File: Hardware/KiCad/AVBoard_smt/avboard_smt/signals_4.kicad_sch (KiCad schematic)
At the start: 20 parts, among them IC2_AUD0 7432N, IC4_AUD0 7400N, IC6_AUD0 7474N, IC7_AUD0 LM358N, U1 W65C02SP

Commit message: update kicad SMT BOMs
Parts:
- AUDJACK0: MPN RCJ-103 -> RCJ-013
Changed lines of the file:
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@@
       (effects (font (size 1.27 1.27)) hide)
     )
-    (property "MPN" "RCJ-103" (at 528.32 43.18 0)
+    (property "MPN" "RCJ-013" (at 528.32 43.18 0)
       (effects (font (size 1.27 1.27)) hide)
     )

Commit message: collect production documents for quoting
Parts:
- MOTHERBOARD0: footprint Connector_FFC-FPC:TE_4-1734839-0_1x40-1MP_P0.5mm_Horizontal -> SamacSys_Parts:F34G1A7Q1E8C40; MPN 4-1734839-0 -> F34G-1A7Q1-E8C40

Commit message: replace dual ported frame buffer with mirrored single ported rams
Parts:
- removed unit 4 of IC2_AUD0
- added IC2: IS61C64AL-10TLI, SOP55P1340X120-28N, symbol SamacSys_Parts:IS61C64AL-10TLI
- added IC3: SN74CBT16245CDGGR, SOP50P810X120-48N, symbol SamacSys_Parts:SN74CBT16245CDGGR
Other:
- note removed: "unused, left unconnected in case needed for bodge work"

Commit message: design out the 4K dualport ram
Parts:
- removed IC3: SN74CBT16245CDGGR, SOP50P810X120-48N, symbol SamacSys_Parts:SN74CBT16245CDGGR
- removed R22: 3.3k, Resistor_SMD:R_0805_2012Metric, symbol signals-eagle-import:R-US_0207/10
- removed U$2: PDPRAM_4KPLCC52S, Package_LCC:PLCC-52_SMD-Socket, symbol signals-eagle-import:PDPRAM_4KPLCC52S
- added IC3: SN74CBT16210CDLR, SOP64P1035X279-48N, symbol SamacSys_Parts:SN74CBT16210CDLR
- added IC4: 74VHC157FT, SOP65P640X120-16N, symbol SamacSys_Parts:74VHC157FT
- added U10: 74AHC373, Package_SO:TSSOP-20_4.4x6.5mm_P0.65mm, symbol 74xx:74AHC373
- IC2: MPN (none) -> IS61C64AL-10TLI; Manufacturer_Part_Number IS61C64AL-10TLI -> (none)
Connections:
- net AA0: now also IC2.10 (A0), IC3.46 (1B1)
- net AA1: now also IC2.9 (A1), IC3.45 (1B2)
- net AA10: now also IC2.21 (A10), IC3.35 (2B1)
- net AA11: now also IC2.23 (A11), IC3.34 (2B2)
- net AA2: now also IC2.8 (A2), IC3.44 (1B3)
- net AA3: now also IC2.7 (A3), IC3.43 (1B4)
- net AA4: now also IC2.6 (A4), IC3.42 (1B5)
- net AA5: now also IC2.5 (A5), IC3.40 (1B6)
- net AA6: now also IC2.4 (A6), IC3.39 (1B7)
- net AA7: now also IC2.3 (A7), IC3.38 (1B8)
- net AA8: now also IC2.25 (A8), IC3.37 (1B9)
- net AA9: now also IC2.24 (A9), IC3.36 (1B10)
- net AD0: now also IC2.11 (I/O0), IC3.33 (2B3), U10.3 (D0)
- net AD1: now also IC2.12 (I/O1), IC3.31 (2B4), U10.4 (D1)
- net AD2: now also IC2.13 (I/O2), IC3.30 (2B5), U10.7 (D2)
- net AD3: now also IC2.15 (I/O3), IC3.29 (2B6), U10.8 (D3)
- net AD4: now also IC2.16 (I/O4), IC3.28 (2B7), U10.13 (D4)
- net AD5: now also IC2.17 (I/O5), IC3.27 (2B8), U10.14 (D5)
- net AD6: now also IC2.18 (I/O6), IC3.26 (2B9), U10.17 (D6)
- net AD7: now also IC2.19 (I/O7), IC3.25 (2B10), U10.18 (D7)
- net AR/~{W}B: now also IC4.3 (1B)
- net CLK14_AUD: now also U1.36 (BE), IC3.47 (2~{OE}), IC3.48 (1~{OE}), IC4.1 (SELECT); no longer IC4_AUD0.12 (I0), IC4_AUD0.13 (I1)
- net GND: now also IC2.14 (GND), IC2.2 (A12), IC2.20 (~{CE}), IC3.17 (GND_2), IC3.32 (GND_3), IC3.41 (GND_4), IC3.8 (GND_1), IC4.11 (3A), IC4.13 (4B), IC4.15 (~{ST}), IC4.6 (2B), IC4.8 (GND), U10.10 (GND)
- net VCC: now also IC2.28 (VDD), IC3.15 (VCC), IC4.14 (4A), IC4.16 (VCC), U10.20 (VCC)
- net at MOTHERBOARD0.21: now also IC3.14 (2A2)
- net at MOTHERBOARD0.22: now also IC3.13 (2A1)
- net at MOTHERBOARD0.23: now also IC3.12 (1A10)
- net at MOTHERBOARD0.24: now also IC3.11 (1A9)
- net at MOTHERBOARD0.25: now also IC3.10 (1A8)
- net at MOTHERBOARD0.26: now also IC3.9 (1A7)
- net at MOTHERBOARD0.27: now also IC3.7 (1A6)
- net at MOTHERBOARD0.28: now also IC3.6 (1A5)
- net at MOTHERBOARD0.29: now also IC3.5 (1A4)
- net at MOTHERBOARD0.30: now also IC3.4 (1A3)
- net at MOTHERBOARD0.31: now also IC3.3 (1A2)
- net at MOTHERBOARD0.32: now also IC3.2 (1A1)
- net at AUD_FLAGS0.9 (8D), MOTHERBOARD0.33: now also IC3.24 (2A10), U10.19 (O7)
- net at AUD_FLAGS0.8 (7D), MOTHERBOARD0.34: now also IC3.23 (2A9), U10.16 (O6)
- net at AUD_FLAGS0.7 (6D), MOTHERBOARD0.35: now also IC3.22 (2A8), U10.15 (O5)
- net at AUD_FLAGS0.6 (5D), MOTHERBOARD0.36: now also IC3.21 (2A7), U10.12 (O4)
- net at AUD_FLAGS0.5 (4D), MOTHERBOARD0.37: now also IC3.20 (2A6), U10.9 (O3)
- net at AUD_FLAGS0.4 (3D), MOTHERBOARD0.38: now also IC3.19 (2A5), U10.6 (O2)
- net at AUD_FLAGS0.3 (2D), MOTHERBOARD0.39: now also IC3.18 (2A4), U10.5 (O1)
- net at AUD_FLAGS0.2 (1D), MOTHERBOARD0.40: now also IC3.16 (2A3), U10.2 (O0)
- net Sys_ARAM_~{WE}: now reaches IC2_AUD0.3 (O)
- net Sys_ARAM_~{WE}: now also IC4.2 (1A)
- net Sys_ARAM_~{OE}: now reaches IC2_AUD0.6 (O)
- net Sys_ARAM_~{OE}: now also IC4.5 (2A), U10.1 (OE)
- net ARAM_~{OE}: now reaches IC2.22 (~{OE})
- net ARAM_~{OE}: now also IC4.7 (2Y)
- net ARAM_~{WE}: now reaches IC2.27 (~{WE})
- net ARAM_~{WE}: now also IC4.4 (1Y)
- new net ACP_ARAM_~{CE}: IC4.10 (3B)
- new net ARAM_~{CE}: IC4.9 (3Y)
- new net Sys_ARAM_buf_read_latch: IC4.12 (4Y), U10.11 (LE)
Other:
- note added: "SELECT LOW - SYSTEM SELECT HIGH - ACP"
- note removed: "dual ported SRAM"
- moved on the sheet: IC2, IC4_AUD0C, IC4_AUD0D, R21

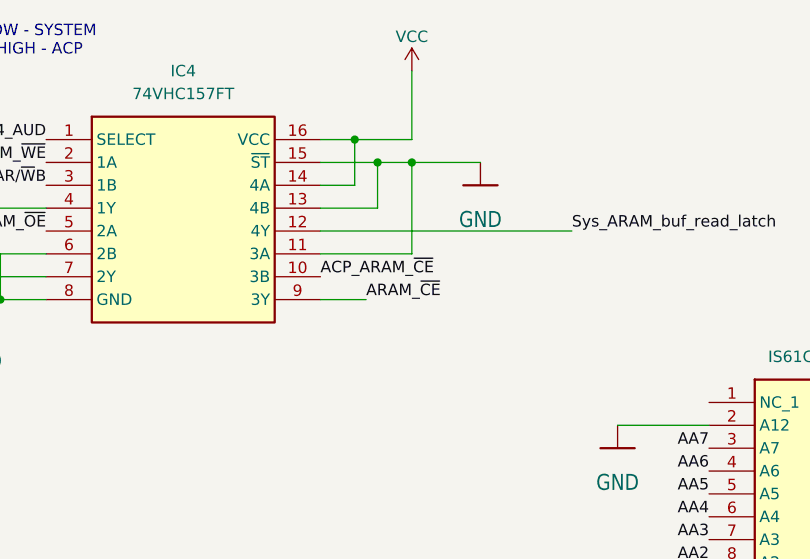
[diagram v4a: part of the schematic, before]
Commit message: connect loose unused inputs to ground
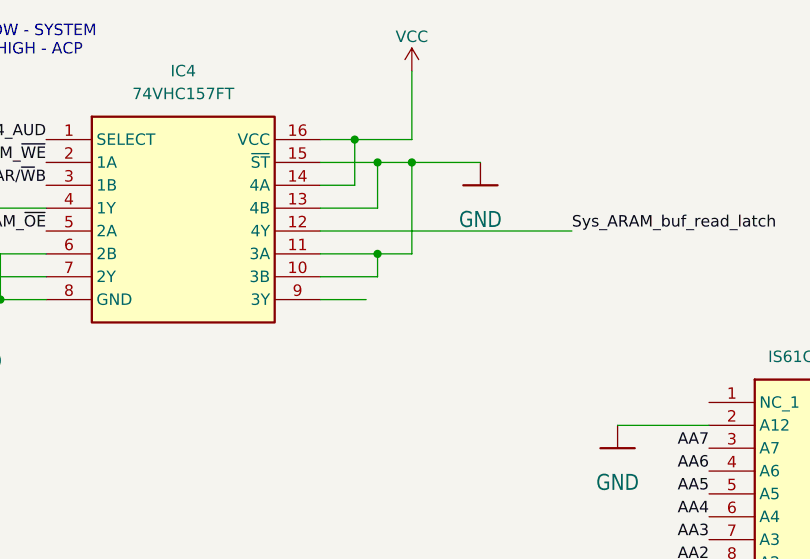
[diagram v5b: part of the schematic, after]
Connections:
- net ACP_ARAM_~{CE} is gone; now on net GND: IC4.10 (3B)
- net ARAM_~{CE}: no longer names the net of IC4.9 (3Y)
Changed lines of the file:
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@@
 	)
 	(junction
+		(at 167.64 -19.05)
+		(diameter 0)
+		(color 0 0 0 0)
+	)
+	(junction
 		(at 175.26 209.55)
 		(diameter 0)
@@
 	(wire
 		(pts
-			(xy 161.29 -19.05) (xy 171.45 -19.05)
+			(xy 161.29 -19.05) (xy 167.64 -19.05)
 		)
 		(stroke
@@
 	(wire
 		(pts
+			(xy 167.64 -19.05) (xy 171.45 -19.05)
+		)
+		(stroke
+			(width 0)
+			(type default)
+		)
+	)
+	(wire
+		(pts
 			(xy -120.65 34.29) (xy -109.22 34.29)
 		)
@@
 	(wire
 		(pts
+			(xy 161.29 -16.51) (xy 167.64 -16.51)
+		)
+		(stroke
+			(width 0)
+			(type default)
+		)
+	)
+	(wire
+		(pts
 			(xy 327.66 137.16) (xy 327.66 167.64)
 		)
@@
 	(wire
 		(pts
+			(xy 167.64 -16.51) (xy 167.64 -19.05)
+		)
+		(stroke
+			(width 0)
+			(type default)
+		)
+	)
+	(wire
+		(pts
 			(xy 181.61 152.4) (xy 259.08 152.4)
 		)
@@
 		)
 	)
-	(label "ACP_ARAM_~{CE}"
-		(at 161.29 -16.51 0)
-		(effects
-			(font
-				(size 1.27 1.27)
-			)
-			(justify left bottom)
-		)
-	)
 	(label "Sys_ARAM_~{WE}"
 		(at 130.81 -29.21 180)
@@
 		)
 	)
-	(label "ARAM_~{CE}"
-		(at 166.37 -13.97 0)
-		(effects
-			(font
-				(size 1.27 1.27)
-			)
-			(justify left bottom)
-		)
-	)

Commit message: Add AV board version with VRAM replaced but not ARAM
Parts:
- removed IC2: IS61C64AL-10TLI, SOP55P1340X120-28N, symbol SamacSys_Parts:IS61C64AL-10TLI
- removed IC3: SN74CBT16210CDLR, SOP64P1035X279-48N, symbol SamacSys_Parts:SN74CBT16210CDLR
- removed IC4: 74VHC157FT, SOP65P640X120-16N, symbol SamacSys_Parts:74VHC157FT
- removed U10: 74AHC373, Package_SO:TSSOP-20_4.4x6.5mm_P0.65mm, symbol 74xx:74AHC373
- added R22: 3.3k, Resistor_SMD:R_0805_2012Metric, symbol signals-eagle-import:R-US_0207/10
- added U$2: PDPRAM_4KPLCC52S, Package_LCC:PLCC-52, symbol signals-eagle-import:PDPRAM_4KPLCC52S
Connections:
- net AA0: now also U$2.45 (AR0)
- net AA1: now also U$2.44 (AR1)
- net AA10: now also U$2.47 (AR10)
- net AA11: now also U$2.48 (AR11)
- net AA2: now also U$2.43 (AR2)
- net AA3: now also U$2.42 (AR3)
- net AA4: now also U$2.41 (AR4)
- net AA5: now also U$2.40 (AR5)
- net AA6: now also U$2.39 (AR6)
- net AA7: now also U$2.38 (AR7)
- net AA8: now also U$2.37 (AR8)
- net AA9: now also U$2.36 (AR9)
- net AD0: now also U$2.27 (DR0)
- net AD1: now also U$2.28 (DR1)
- net AD2: now also U$2.29 (DR2)
- net AD3: now also U$2.30 (DR3)
- net AD4: now also U$2.31 (DR4)
- net AD5: now also U$2.32 (DR5)
- net AD6: now also U$2.33 (DR6)
- net AD7: now also U$2.34 (DR7)
- net AR/~{W}B: now also U$2.50 (R/_WR)
- net CLK14_AUD: now also IC4_AUD0.12 (I0), IC4_AUD0.13 (I1); no longer U1.36 (BE)
- net GND: now also U$2.1 (_CEL), U$2.26 (GND), U$2.46 (_OER)
- net VCC: now also R22.2, U$2.3 (_SEML), U$2.49 (_SEMR), U$2.52 (VCC)
- net at AUD_FLAGS0.6 (5D), MOTHERBOARD0.36: now also U$2.21 (DL4)
- net at AUD_FLAGS0.7 (6D), MOTHERBOARD0.35: now also U$2.22 (DL5)
- net at AUD_FLAGS0.8 (7D), MOTHERBOARD0.34: now also U$2.23 (DL6)
- net at AUD_FLAGS0.9 (8D), MOTHERBOARD0.33: now also U$2.24 (DL7)
- net at AUD_FLAGS0.2 (1D), MOTHERBOARD0.40: now also U$2.17 (DL0)
- net at AUD_FLAGS0.3 (2D), MOTHERBOARD0.39: now also U$2.18 (DL1)
- net at AUD_FLAGS0.4 (3D), MOTHERBOARD0.38: now also U$2.19 (DL2)
- net at AUD_FLAGS0.5 (4D), MOTHERBOARD0.37: now also U$2.20 (DL3)
- net at IC4_AUD0.11 (O): now also U$2.51 (_CER)
- net at MOTHERBOARD0.21: now also U$2.4 (AL11)
- net at MOTHERBOARD0.22: now also U$2.5 (AL10)
- net at MOTHERBOARD0.23: now also U$2.16 (AL9)
- net at MOTHERBOARD0.24: now also U$2.15 (AL8)
- net at MOTHERBOARD0.25: now also U$2.14 (AL7)
- net at MOTHERBOARD0.26: now also U$2.13 (AL6)
- net at MOTHERBOARD0.27: now also U$2.12 (AL5)
- net at MOTHERBOARD0.28: now also U$2.11 (AL4)
- net at MOTHERBOARD0.29: now also U$2.10 (AL3)
- net at MOTHERBOARD0.30: now also U$2.9 (AL2)
- net at MOTHERBOARD0.31: now also U$2.8 (AL1)
- net at MOTHERBOARD0.32: now also U$2.7 (AL0)
- net Sys_ARAM_~{OE}: no longer names the net of IC2_AUD0.6 (O)
- net Sys_ARAM_~{OE}: now also U$2.6 (_OEL)
- net Sys_ARAM_~{WE}: no longer names the net of IC2_AUD0.3 (O)
- net Sys_ARAM_~{WE}: now also U$2.2 (R/_WL)
- new net: R22.1, U1.36 (BE)
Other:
- note added: "dual ported SRAM"
- note removed: "SELECT LOW - SYSTEM SELECT HIGH - ACP"
- moved on the sheet: IC4_AUD0C, IC4_AUD0D, R21

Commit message: updates
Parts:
- AUDJACK0: value RCJ-014 -> RCJ-012; MPN RCJ-013 -> RCJ-012
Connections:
- net SysA11: now reaches MOTHERBOARD0.21, U$2.4 (AL11)
- net SysA10: now reaches MOTHERBOARD0.22, U$2.5 (AL10)
- net SysA9: now reaches MOTHERBOARD0.23, U$2.16 (AL9)
- net SysA8: now reaches MOTHERBOARD0.24, U$2.15 (AL8)
- net SysA7: now reaches MOTHERBOARD0.25, U$2.14 (AL7)
- net SysA6: now reaches MOTHERBOARD0.26, U$2.13 (AL6)
- net SysA5: now reaches MOTHERBOARD0.27, U$2.12 (AL5)
- net SysA4: now reaches MOTHERBOARD0.28, U$2.11 (AL4)
- net SysA3: now reaches MOTHERBOARD0.29, U$2.10 (AL3)
- net SysA2: now reaches MOTHERBOARD0.30, U$2.9 (AL2)
- net SysA1: now reaches MOTHERBOARD0.31, U$2.8 (AL1)
- net SysA0: now reaches MOTHERBOARD0.32, U$2.7 (AL0)
- net SysD7: now reaches AUD_FLAGS0.9 (8D), MOTHERBOARD0.33, U$2.24 (DL7)
- net SysD6: now reaches AUD_FLAGS0.8 (7D), MOTHERBOARD0.34, U$2.23 (DL6)
- net SysD5: now reaches AUD_FLAGS0.7 (6D), MOTHERBOARD0.35, U$2.22 (DL5)
- net SysD4: now reaches AUD_FLAGS0.6 (5D), MOTHERBOARD0.36, U$2.21 (DL4)
- net SysD3: now reaches AUD_FLAGS0.5 (4D), MOTHERBOARD0.37, U$2.20 (DL3)
- net SysD2: now reaches AUD_FLAGS0.4 (3D), MOTHERBOARD0.38, U$2.19 (DL2)
- net SysD1: now reaches AUD_FLAGS0.3 (2D), MOTHERBOARD0.39, U$2.18 (DL1)
- net at AUD_FLAGS0.2 (1D), MOTHERBOARD0.40, U$2.17 (DL0): no longer names the net of AUD_FLAGS0.2 (1D), MOTHERBOARD0.40, U$2.17 (DL0)
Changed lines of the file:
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@@
 	(text "op amp power pins"
 		(exclude_from_sim no)
-		(at 441.96 96.52 0)
+		(at -110.49 85.09 0)
 		(effects
 			(font
@@
 		)
 	)
+	(label "SysD0"
+		(at 139.7 165.1 0)
+		(effects
+			(font
+				(size 1.27 1.27)
+			)
+			(justify left bottom)
+		)
+	)
 	(label "AA4"
 		(at 182.88 142.24 0)
@@
 		)
 	)
+	(label ""
+		(at 127 128.27 0)
+		(effects
+			(font
+				(size 1.27 1.27)
+			)
+			(justify left bottom)
+		)
+	)
 	(label "AUD_REG2"
 		(at 63.5 66.04 270)
@@
 		)
 	)
+	(label "SysD3"
+		(at 139.7 172.72 0)
+		(effects
+			(font
+				(size 1.27 1.27)
+			)
+			(justify left bottom)
+		)
+	)
+	(label "SysD4"
+		(at 139.7 175.26 0)
+		(effects
+			(font
+				(size 1.27 1.27)
+			)
+			(justify left bottom)
+		)
+	)
+	(label "SysD5"
+		(at 139.7 177.8 0)
+		(effects
+			(font
+				(size 1.27 1.27)
+			)
+			(justify left bottom)
+		)
+	)
+	(label "SysD6"
+		(at 139.7 180.34 0)
+		(effects
+			(font
+				(size 1.27 1.27)
+			)
+			(justify left bottom)
+		)
+	)
+	(label "SysD7"
+		(at 139.7 182.88 0)
+		(effects
+			(font
+				(size 1.27 1.27)
+			)
+			(justify left bottom)
+		)
+	)
+	(label "SysD2"
+		(at 139.7 170.18 0)
+		(effects
+			(font
+				(size 1.27 1.27)
+			)
+			(justify left bottom)
+		)
+	)
+	(label "SysD1"
+		(at 139.7 167.64 0)
+		(effects
+			(font
+				(size 1.27 1.27)
+			)
+			(justify left bottom)
+		)
+	)
 	(label "AR/~{W}B"
 		(at 229.235 187.96 180)
@@
 		)
 	)
+	(label "SysA0"
+		(at 139.7 132.08 0)
+		(effects
+			(font
+				(size 1.27 1.27)
+			)
+			(justify left bottom)
+		)
+	)
+	(label "SysA1"
+		(at 139.7 134.62 0)
+		(effects
+			(font
+				(size 1.27 1.27)
+			)
+			(justify left bottom)
+		)
+	)
+	(label "SysA4"
+		(at 139.7 142.24 0)
+		(effects
+			(font
+				(size 1.27 1.27)
+			)
+			(justify left bottom)
+		)
+	)
+	(label "SysA2"
+		(at 139.7 137.16 0)
+		(effects
+			(font
+				(size 1.27 1.27)
+			)
+			(justify left bottom)
+		)
+	)
+	(label "SysA3"
+		(at 139.7 139.7 0)
+		(effects
+			(font
+				(size 1.27 1.27)
+			)
+			(justify left bottom)
+		)
+	)
+	(label "SysA9"
+		(at 139.7 154.94 0)
+		(effects
+			(font
+				(size 1.27 1.27)
+			)
+			(justify left bottom)
+		)
+	)
+	(label "SysA5"
+		(at 139.7 144.78 0)
+		(effects
+			(font
+				(size 1.27 1.27)
+			)
+			(justify left bottom)
+		)
+	)
+	(label "SysA6"
+		(at 139.7 147.32 0)
+		(effects
+			(font
+				(size 1.27 1.27)
+			)
+			(justify left bottom)
+		)
+	)
+	(label "SysA7"
+		(at 139.7 149.86 0)
+		(effects
+			(font
+				(size 1.27 1.27)
+			)
+			(justify left bottom)
+		)
+	)
+	(label "SysA8"
+		(at 139.7 152.4 0)
+		(effects
+			(font
+				(size 1.27 1.27)
+			)
+			(justify left bottom)
+		)
+	)
+	(label "SysA11"
+		(at 139.7 160.02 0)
+		(effects
+			(font
+				(size 1.27 1.27)
+			)
+			(justify left bottom)
+		)
+	)
+	(label "SysA10"
+		(at 139.7 157.48 0)
+		(effects
+			(font
+				(size 1.27 1.27)
+			)
+			(justify left bottom)
+		)
+	)
 	(label "AUD_REG0"
 		(at 68.58 66.04 270)
@@
 	(symbol
 		(lib_id "signals-eagle-import:GND")
-		(at 436.88 104.14 0)
+		(at -115.57 92.71 0)
 		(unit 1)
 		(exclude_from_sim no)
@@
 		(dnp no)
 		(property "Reference" "#GND023"
-			(at 436.88 104.14 0)
+			(at -115.57 92.71 0)
 			(effects
 				(font
@@
 		)
 		(property "Value" "GND"
-			(at 434.34 106.68 0)
+			(at -118.11 95.25 0)
 			(effects
 				(font
@@
 		)
 		(property "Footprint" ""
-			(at 436.88 104.14 0)
+			(at -115.57 92.71 0)
 			(effects
 				(font
@@
 		)
 		(property "Datasheet" ""
-			(at 436.88 104.14 0)
+			(at -115.57 92.71 0)
 			(effects
 				(font
@@
 		)
 		(property "Description" ""
-			(at 436.88 104.14 0)
+			(at -115.57 92.71 0)
 			(effects
 				(font
@@
 		)
 		(property "Description" "4K Dual Port SRAM - Clydeware LLC will provide this part"
-			(at 165.1 165.1 0)
+			(at 166.116 121.666 0)
 			(effects
 				(font
@@
 			)
 		)
-		(property "Value" "RCJ-014"
+		(property "Value" "RCJ-012"
 			(at 530.863 36.8223 0)
 			(effects
@@
 			)
 		)
-		(property "MPN" "RCJ-013"
+		(property "MPN" "RCJ-012"
 			(at 528.32 43.18 0)
 			(effects
@@
 	(symbol
 		(lib_id "signals-eagle-import:VCC")
-		(at 436.88 83.82 0)
+		(at -115.57 72.39 0)
 		(unit 1)
 		(exclude_from_sim no)
@@
 		(dnp no)
 		(property "Reference" "#P+013"
-			(at 436.88 83.82 0)
+			(at -115.57 72.39 0)
 			(effects
 				(font
@@
 		)
 		(property "Value" "VCC"
-			(at 434.34 86.36 90)
+			(at -118.11 74.93 90)
 			(effects
 				(font
@@
 		)
 		(property "Footprint" ""
-			(at 436.88 83.82 0)
+			(at -115.57 72.39 0)
 			(effects
 				(font
@@
 		)
 		(property "Datasheet" ""
-			(at 436.88 83.82 0)
+			(at -115.57 72.39 0)
 			(effects
 				(font
@@
 		)
 		(property "Description" ""
-			(at 436.88 83.82 0)
+			(at -115.57 72.39 0)
 			(effects
 				(font
@@
 	(symbol
 		(lib_id "signals-eagle-import:LM358N")
-		(at 436.88 93.98 0)
+		(at -115.57 82.55 0)
 		(unit 3)
 		(exclude_from_sim no)
@@
 		(dnp no)
 		(property "Reference" "IC7_AUD0"
-			(at 439.42 90.805 0)
+			(at -113.03 79.375 0)
 			(effects
 				(font
@@
 		)
 		(property "Value" "LM358N"
-			(at 439.42 99.06 0)
+			(at -113.03 87.63 0)
 			(effects
 				(font
@@
 		)
 		(property "Footprint" "Package_SO:TSSOP-8_4.4x3mm_P0.65mm"
-			(at 436.88 93.98 0)
+			(at -115.57 82.55 0)
 			(effects
 				(font
@@
 		)
 		(property "Datasheet" ""
-			(at 436.88 93.98 0)
+			(at -115.57 82.55 0)
 			(effects
 				(font
@@
 		)
 		(property "Description" ""
-			(at 436.88 93.98 0)
+			(at -115.57 82.55 0)
 			(effects
 				(font
@@
 		)
 		(property "MPN" "LM358APWR"
-			(at 436.88 93.98 0)
+			(at -115.57 82.55 0)
 			(effects
 				(font
